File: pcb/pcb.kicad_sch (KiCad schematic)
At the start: 51 parts, among them J1 Ribbon Cable Header, J2 Ribbon Cable Header, J3 ISP, SW1 Cherry MX Grey Switch w/ Gree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, SW2 Cherry MX Grey Switch w/ Gree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, SW3 1241.1100.7095, SW4 SW_SPST, U1 Display Driver, U2 Display Driver, U3 MCU, U4 Inverter, 3 Channels, U5 3:8 Demux, U6 NOR, 4 Channels, U7 OR, 2 Channels, U8 5V Buck Voltage Regulator, Y1 20MHz

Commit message: crush every error
Signed-off-by: Michael Darr <michael.e.darr@gmail.com>
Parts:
- SW1, SW2: value Cherry MX Grey Switch w/ Green LED -> MX Grey w/ LED
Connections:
- net GND: now also J1.13; no longer C1.1, C2.1, J1.14, J2.14, U1.35 (GND), U2.35 (GND), U2.36 (OSCILLATOR)
- net VCC: now also J1.2; no longer C1.2, C2.2, J1.11, J2.11, U1.1 (V+), U2.1 (V+)
- net bp: now also J2.11; no longer J1.13, J2.13, U4.6 (IN_A3)
- net col1: no longer J1.1, U7.7 (1Y)
- net cs_1_1: now also J2.4; no longer J1.12, J2.12, U5.15 (Y0)
- net cs_1_2: now also J2.12; no longer J1.3, J2.3, U5.14 (Y1)
- net data_0: no longer J2.10, U1.27 (B0), U2.27 (B0)
- net data_1: no longer J2.9, U1.28 (B1), U2.28 (B1)
- net data_2: no longer J2.8, U1.29 (B2), U2.29 (B2)
- net data_3: no longer J2.7, U1.30 (B3), U2.30 (B3)
- net digit_1: no longer J2.6, U1.31 (DIGIT_SELECT_1), U2.31 (DIGIT_SELECT_1)
- net digit_2: no longer J2.5, U1.32 (DIGIT_SELECT_2), U2.32 (DIGIT_SELECT_2)
- net mux_b: now also J1.3; no longer J1.4, J2.4, U1.34 (~{CHIP_SELECT_2}), U2.34 (~{CHIP_SELECT_2})
- net ~{bp}: now also J2.14; no longer J1.2, J2.2, U4.2 (OUT_~{Y3}), U7.1 (1A)
- new net VDD: C1.2, C2.2, J2.2, U1.1 (V+), U2.1 (V+)
- new net VSS: C1.1, C2.1, J2.13, U1.35 (GND), U2.35 (GND), U2.36 (OSCILLATOR)
- new net col1_bp: J1.1, U7.7 (1Y)
- new net cs_2: J2.3, U1.34 (~{CHIP_SELECT_2}), U2.34 (~{CHIP_SELECT_2})
- new net d0: J2.10, U1.27 (B0), U2.27 (B0)
- new net d1: J2.9, U1.28 (B1), U2.28 (B1)
- new net d2: J2.8, U1.29 (B2), U2.29 (B2)
- new net d3: J2.7, U1.30 (B3), U2.30 (B3)
- new net ds_1: J2.6, U1.31 (DIGIT_SELECT_1), U2.31 (DIGIT_SELECT_1)
- new net ds_2: J2.5, U1.32 (DIGIT_SELECT_2), U2.32 (DIGIT_SELECT_2)
- new net lcd1_write: J1.4, U5.15 (Y0)
- new net lcd2_write: J1.12, U5.14 (Y1)
- new net lcd_bp: J1.11, U4.6 (IN_A3)
- new net ~{lcd_bp}: J1.14, U4.2 (OUT_~{Y3}), U7.1 (1A)
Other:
- moved on the sheet: C1, C2, C5, J1, J2, LCD1, LCD2, LS1, U1, U2

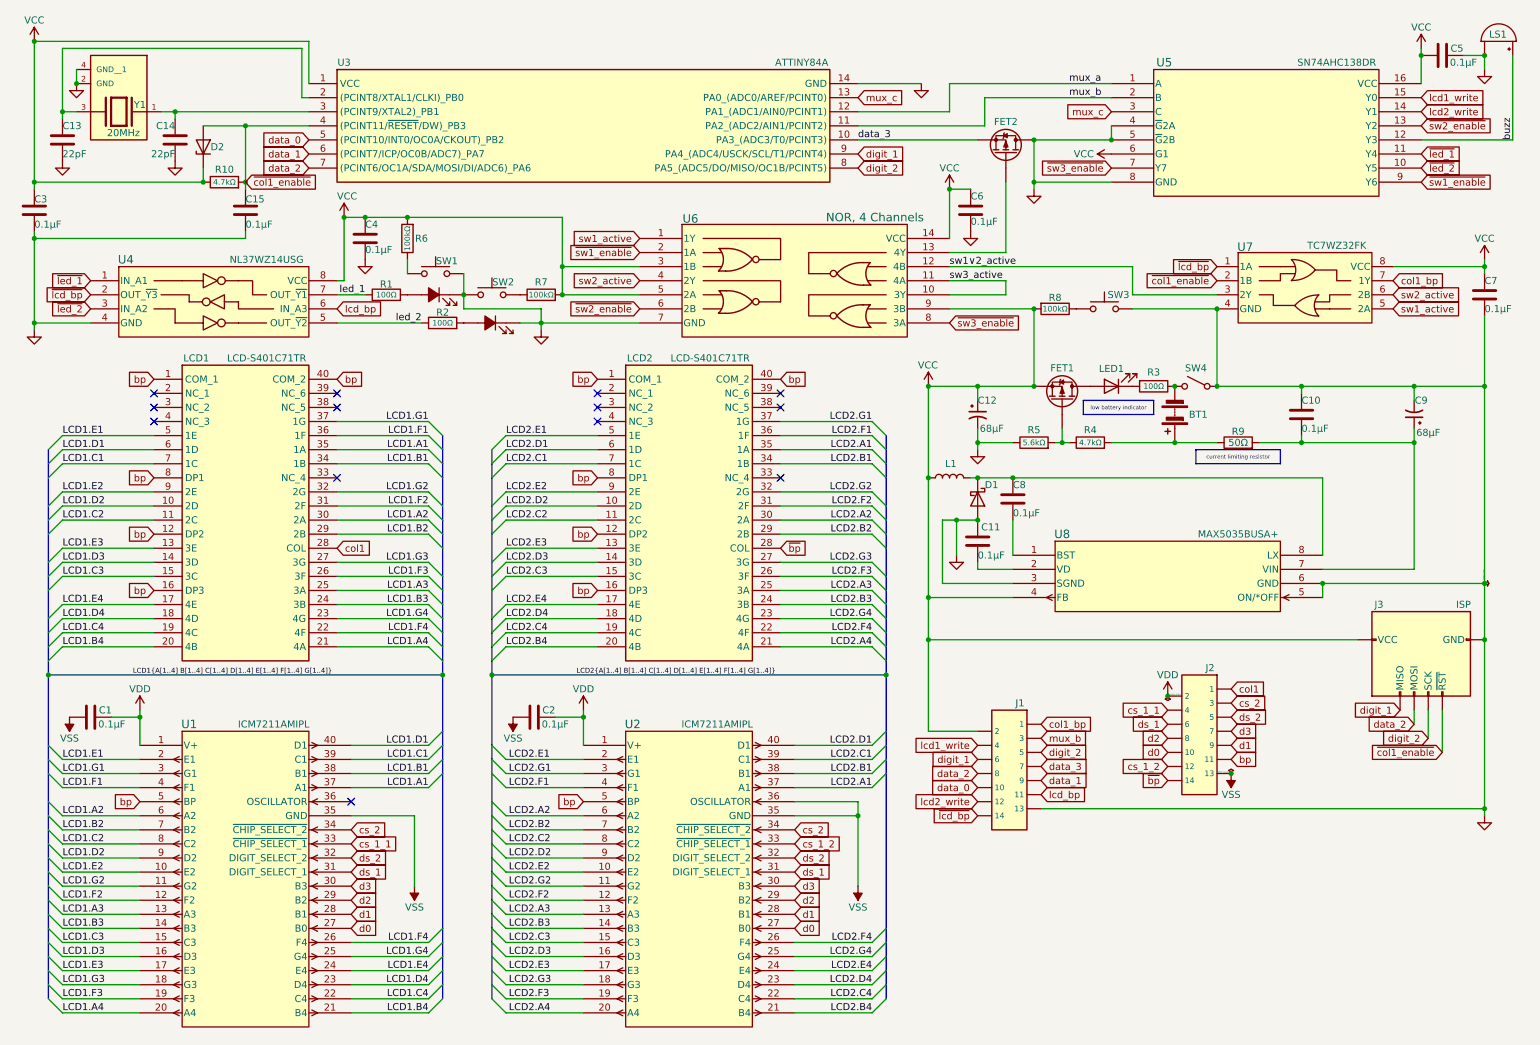
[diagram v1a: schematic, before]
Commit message: narrow down schematic for v0.2.0
Signed-off-by: Michael Darr <michael.e.darr@gmail.com>
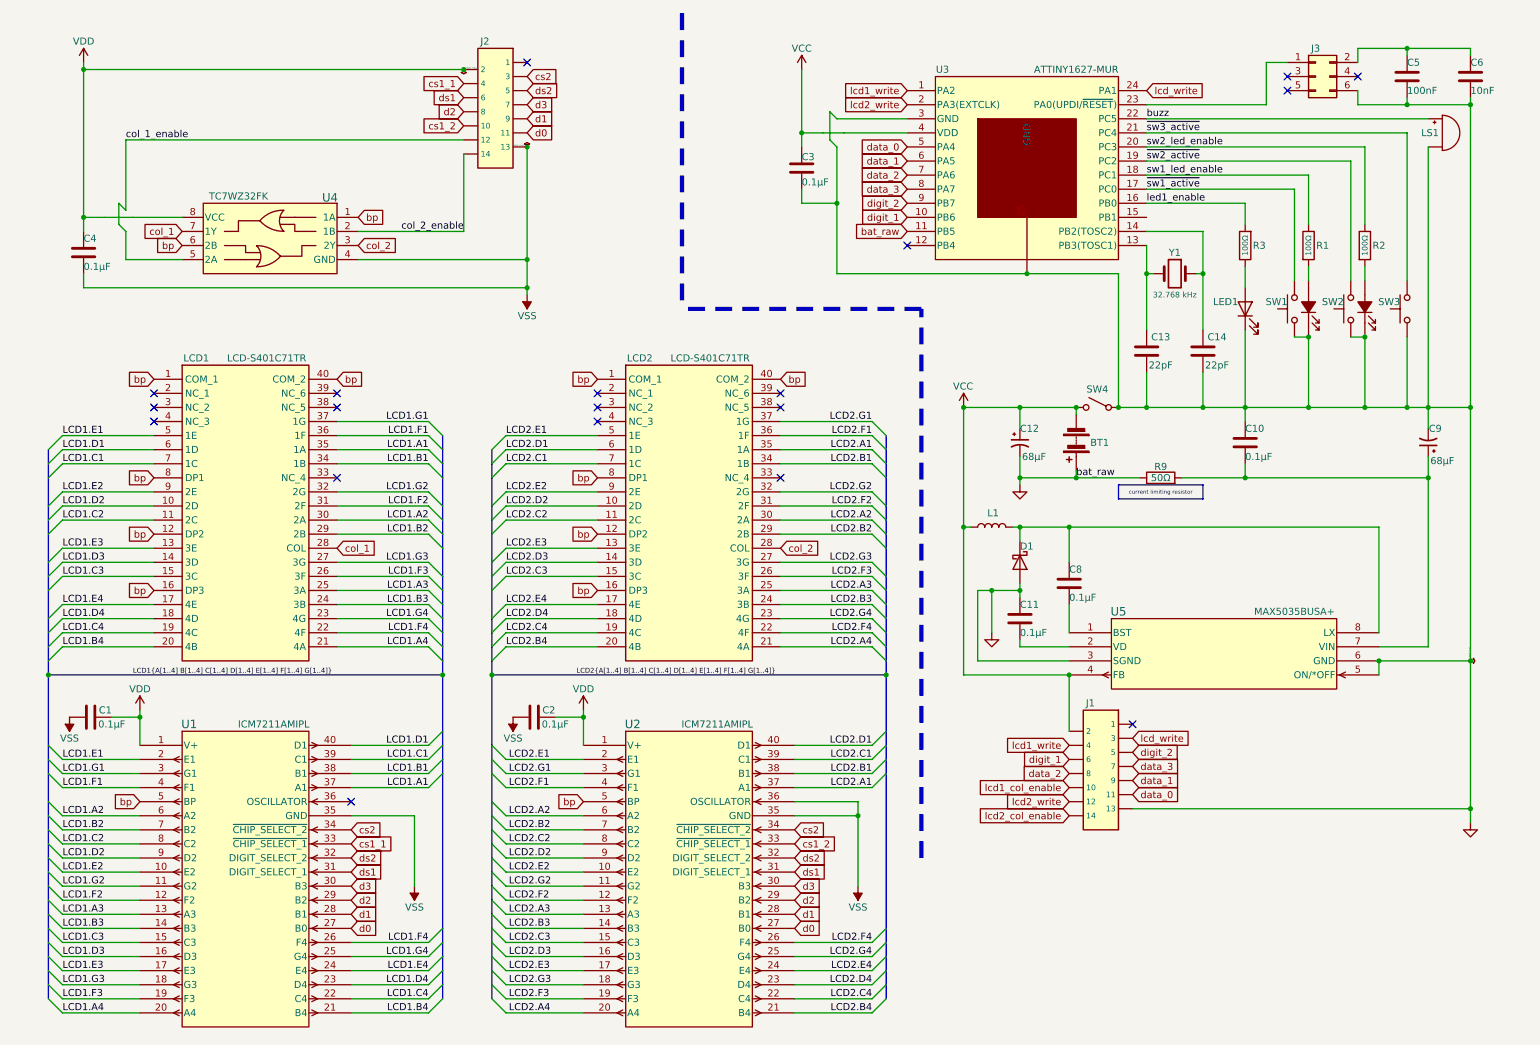
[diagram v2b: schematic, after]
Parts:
- removed C15, C4: 0.1µF, Capacitor_SMD:C_0805_2012Metric_Pad1.18x1.45mm_HandSolder, symbol Device:C
- removed D2: TVS Diode, Diode_SMD:D_SOD-523, symbol Device:D_Zener
- removed FET1, FET2: PMOS, Package_TO_SOT_THT:TO-220-3_Vertical, symbol Simulation_SPICE:PMOS
- removed J3: ISP, Connector_PinHeader_2.54mm:PinHeader_2x03_P2.54mm_Vertical, symbol Connector:AVR-ISP-6
- removed R10, R4: 4.7kΩ, Resistor_SMD:R_0805_2012Metric_Pad1.20x1.40mm_HandSolder, symbol Device:R
- removed R5: 5.6kΩ, Resistor_SMD:R_0805_2012Metric_Pad1.20x1.40mm_HandSolder, symbol Device:R
- removed R6, R7, R8: 100kΩ, Resistor_SMD:R_0805_2012Metric_Pad1.20x1.40mm_HandSolder, symbol Device:R
- removed U4: Inverter, 3 Channels, chess_clock:NL37WZ14USG, symbol Clock-Parts:NL37WZ14USG
- removed U5: 3:8 Demux, chess_clock:SN74AHC138DR, symbol Clock-Parts:SN74AHC138DR
- removed U6: NOR, 4 Channels, chess_clock:SN74F02D, symbol Clock-Parts:SN74F02D
- added J3: ~, Connector_PinHeader_2.54mm:PinHeader_2x03_P2.54mm_Vertical, symbol Connector_Generic:Conn_02x03_Odd_Even
- C5: value 0.1µF -> 100nF; footprint Capacitor_SMD:C_0805_2012Metric_Pad1.18x1.45mm_HandSolder -> (none); Notes 0805 package -> (none); PN CL21B104KBCNNNC -> (none)
- C6: value 0.1µF -> 10nF; footprint Capacitor_SMD:C_0805_2012Metric_Pad1.18x1.45mm_HandSolder -> (none); Notes 0805 package -> (none); PN CL21B104KBCNNNC -> (none)
- U3: footprint chess_clock:ATtiny84a -> chess_clock:ATTINY1627; symbol Clock-Parts:ATTINY44A-PU -> Clock-Parts:ATTINY1627-MUR; PN ATTINY84A -> ATTINY1627-MUR
- Y1: value 20MHz -> 32.768 kHz; footprint chess_clock:ABM8-20.000MHZ-10-B1U-T -> chess_clock:CM315D32768HZFT; symbol Clock-Parts:ABM8-20.000MHZ-10-B1U-T -> Device:Crystal; PN ABM8-20.000MHZ-10-B1U-T -> CM315D32768HZFT
- renumbered C7 to C4, U7 to U4, U8 to U5
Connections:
- net lcd_bp is gone; now on net data_0: J1.11
- net sw1_active is gone; now on net col_1_enable: U4.5 (2A)
- net sw2_active is gone; now on net bp: U4.6 (2B)
- net GND: now also BT1.1 (+), LED1.1 (K), R9.1, SW2.1, SW3.1, U3.11 (PB5), U3.25 (GND), U3.3 (GND), J3.6 (Pin_6); no longer C4.2, SW2.2, SW3.2, U3.14 (GND), U4.4 (GND), Y1.2 (GND), Y1.4 (GND__1)
- net VCC: now also BT1.2 (-), SW4.2 (B), U3.4 (VDD); no longer C4.1, C5.1, C6.1, U3.1 (VCC), U4.8 (VCC)
- net VDD: now also C4.1, U4.8 (VCC)
- net VSS: now also C4.2, U4.4 (GND)
- net bp: now also U4.1 (1A); no longer J2.11
- net buzz: now also U3.22 (PC5)
- net d0: now also J2.11; no longer J2.10
- net data_0: no longer J1.10
- net data_3: now also U3.8 (PA7); no longer U3.10 (PA3_(ADC3/T0/PCINT3))
- net digit_1: now also U3.10 (PB6); no longer U3.9 (PA4_(ADC4/USCK/SCL/T1/PCINT4))
- net digit_2: now also U3.9 (PB7); no longer U3.8 (PA5_(ADC5/DO/MISO/OC1B/PCINT5))
- net lcd1_write: now also U3.1 (PA2)
- net lcd2_write: now also U3.2 (PA3(EXTCLK))
- net led1_enable: now reaches R3.2
- net led1_enable: now also U3.16 (PB0); no longer LED1.1 (K)
- net at C14.2, Y1.1: now also U3.14 (PB2(TOSC2)); no longer U3.3 ((PCINT9/XTAL2)_PB1)
- net ~{sw1_active}: now reaches SW1.2
- net ~{sw1_active}: now also U3.17 (PC0)
- net at LED1.2 (A): now also R3.1
- net col1: no longer names the net of J2.1
- net col1: no longer LCD1.28 (COL)
- net col1_bp: no longer names the net of J1.1
- net col1_bp: no longer U4.7 (1Y)
- net cs_1_1 renamed cs1_1
- net cs_1_2 renamed col_1_enable
- net col_1_enable: no longer U2.33 (~{CHIP_SELECT_1})
- net cs_2 renamed cs2
- net ds_1 renamed ds1
- net ds_2 renamed ds2
- net led_1 renamed sw1_led_enable
- net sw1_led_enable: now also U3.18 (PC1)
- net led_2 renamed sw2_led_enable
- net sw2_led_enable: now also U3.20 (PC3)
- net mux_a: no longer names the net of U3.12 (PB4)
- net mux_b renamed lcd_write
- net lcd_write: now also U3.24 (PA1); no longer U3.11 (PA2_(ADC2/AIN1/PCINT2))
- net mux_c: no longer names the net of U3.13 (PB3(TOSC1))
- net mux_c: now also C13.2, Y1.2
- net sw1∨2_active renamed col_2
- net col_2: now also LCD2.28 (COL)
- net ~{bp} renamed col_2_enable
- net col_2_enable: now also U4.2 (1B); no longer LCD2.28 (COL)
- removed net ~{col1_enable}: U3.4 ((PCINT11/~{RESET}/DW)_PB3), U4.2 (1B)
- net ~{lcd_bp} renamed lcd2_col_enable
- net lcd2_col_enable: no longer U4.1 (1A)
- new net: J3.1 (Pin_1), U3.23 (PA0(UPDI/~{RESET}))
- new net: C5.1, C6.1, J3.2 (Pin_2)
- new net col_1: LCD1.28 (COL), U4.7 (1Y)
- new net cs1_2: J2.10, U2.33 (~{CHIP_SELECT_1})
- new net lcd1_col_enable: J1.10
- new net ~{sw2_active}: SW2.2, U3.19 (PC2)
- new net ~{sw3_active}: SW3.2, U3.21 (PC4)
- no-connect marks 13 -> 19
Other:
- moved on the sheet: BT1, C10, C11, C12, C13, C14, C3, C4, C8, C9, D1, J1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
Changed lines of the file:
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@@
     (title "Liclock")
     (date "2023-12-12")
-    (rev "0,6")
+    (rev "0.2.0")
     (company "Radish")
   )

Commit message: Fix violations
Signed-off-by: Michael Darr <michael.e.darr@gmail.com>
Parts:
- C10: renamed from C5; footprint (none) -> Capacitor_SMD:C_0805_2012Metric_Pad1.18x1.45mm_HandSolder; Notes (none) -> 0805 package
- C11: renamed from C6; footprint (none) -> Capacitor_SMD:C_0805_2012Metric_Pad1.18x1.45mm_HandSolder; Notes (none) -> 0805 package
- J3: value ~ -> UPDI; PN (none) -> 10129381-906002BLF
- renumbered C13 to C12, C14 to C13, C8 to C5, C10 to C6, C11 to C7, C12 to C8, R9 to R4
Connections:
- net GND: no longer BT1.1 (+), R4.1, U3.11 (PB5)
- net VCC: no longer BT1.2 (-), SW4.2 (B)
- net lcd1_col_enable: now also U3.12 (PB4)
- net lcd2_col_enable: now also U3.11 (PB5)
- net bat_raw: now reaches U3.15 (PB1)
- net bat_raw: now also BT1.1 (+), R4.1
- new net: BT1.2 (-), SW4.2 (B)
- no-connect marks 19 -> 18
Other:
- moved on the sheet: C3, C4, J2, U4
